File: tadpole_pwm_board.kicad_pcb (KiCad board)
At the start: 2 copper layers, 43.8 x 44.8 mm, 19 parts, among them J1 Conn_01x10_Socket, J10 Conn_01x04_Socket, J11 Conn_01x04_Socket, J9 Conn_01x06_Socket, SW1 SW_Push, SW2 SW_DIP_x06, U1 PCA9685PW, U3 ATtiny85-20S

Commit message: silkscreen work and remaining routing
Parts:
- added G***: LOGO, LOGO, B.Cu at (128.1, 111.3)
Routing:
- net GND: track 19.9 -> 29.1 mm, vias 10 -> 13
- net /RESET: track 39.3 -> 42.9 mm
- net +5V: track 0.00 -> 2.95 mm, vias 0 -> 2
- net /SCL/SCK: track 66.2 -> 64.4 mm
- net /A5: track 31.9 -> 32.8 mm
- net /PWM5: track 11.8 -> 12.6 mm
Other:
- board text added: "FLASH"
- board text added: "I2C ADDR"
- board text added: "PWM OUT"
- board text added: "RESET"
- board text added: "STEMMA"
- board text added: "SYSTEM FAILURE"
- board text added: "TODO: ADD LOGO CHOOSE SWITCH MOUNTING HOLES"
- board text added: "Tadpole ESC Driver Designed by Cooper Jones 9/26/2026"
- board text added: "{dblquote}I'ts me{dblquote}"
- board text removed: "Tadpole PWM thruster control board"

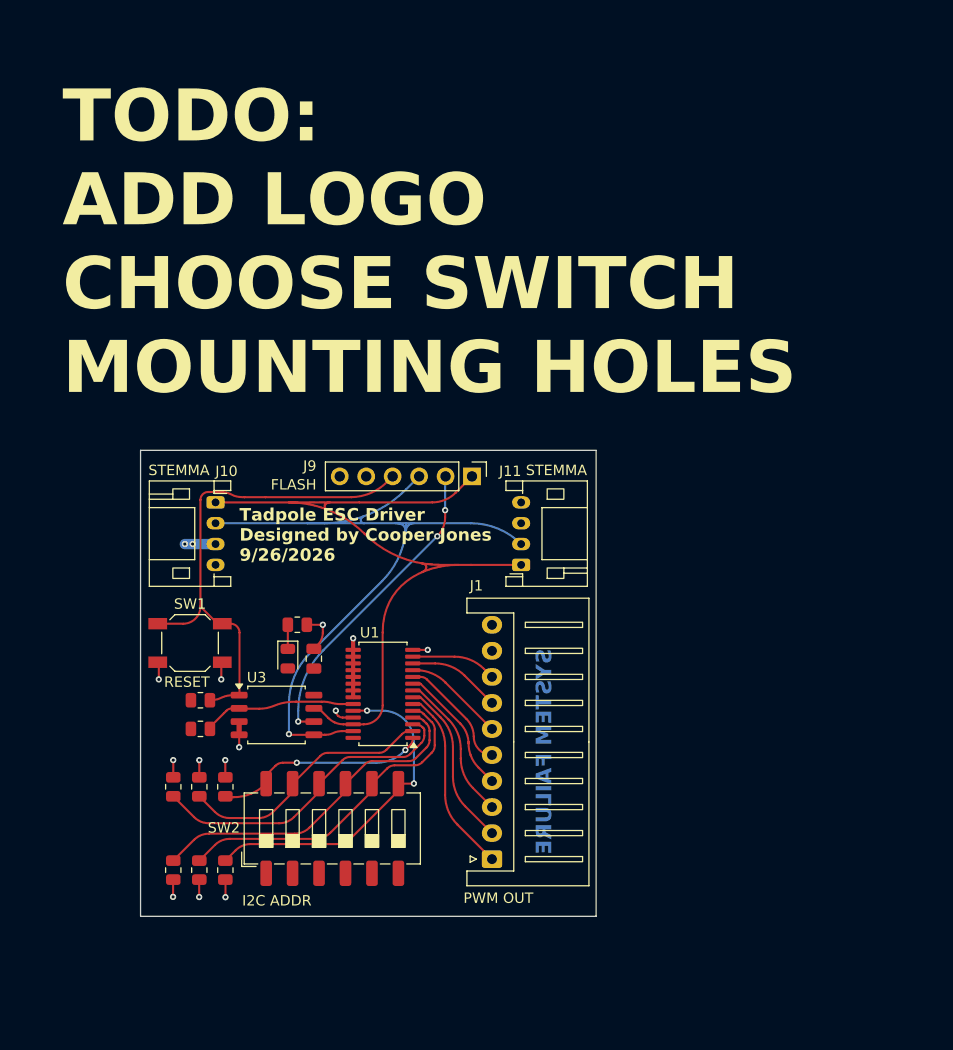
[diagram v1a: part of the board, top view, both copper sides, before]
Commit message: mounting holes, logos, labels, replaced switch
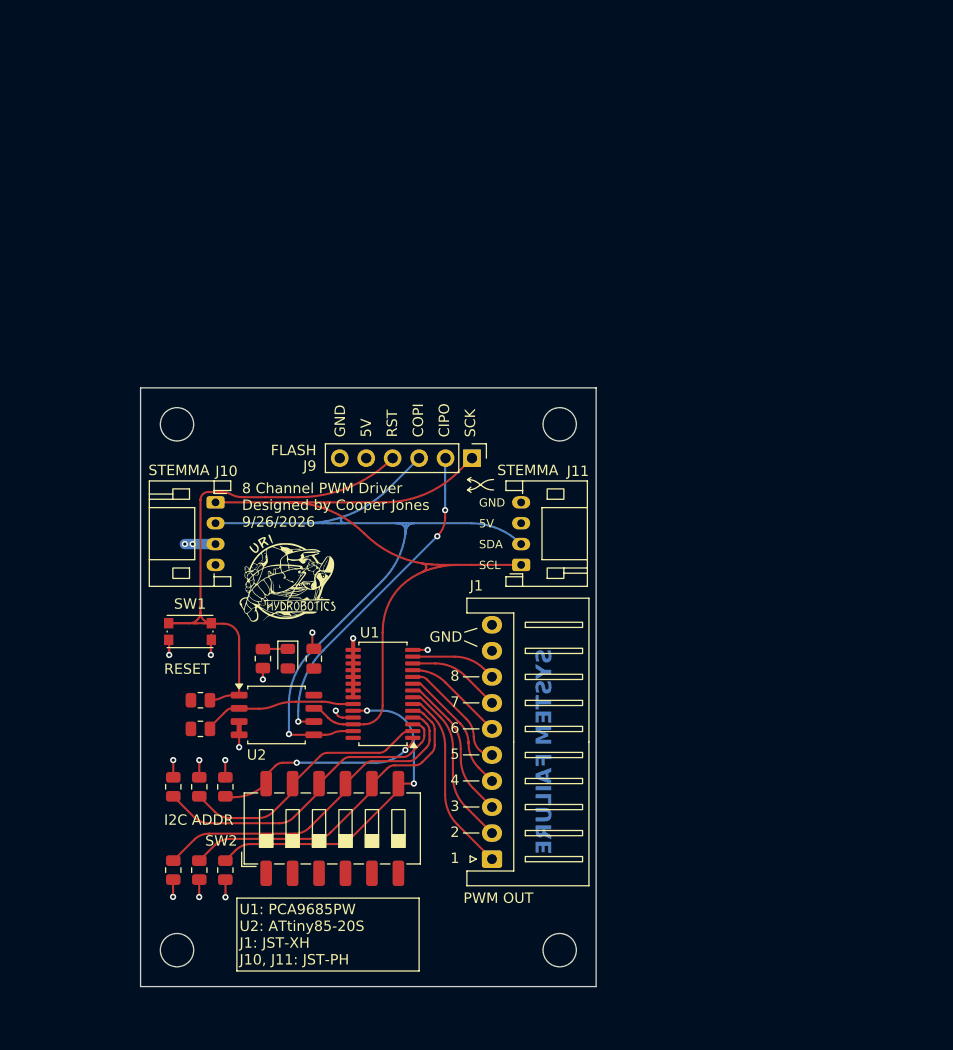
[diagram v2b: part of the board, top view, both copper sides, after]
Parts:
- added G***: LOGO, LOGO, F.Cu at (135.9, 90.2)
- added H1: MountingHole, MountingHole:MountingHole_3.2mm_M3, F.Cu at (125.8, 75.0)
- added H2: MountingHole, MountingHole:MountingHole_3.2mm_M3, F.Cu at (162.5, 75.0)
- added H3: MountingHole, MountingHole:MountingHole_3.2mm_M3, F.Cu at (125.8, 125.5)
- added H4: MountingHole, MountingHole:MountingHole_3.2mm_M3, F.Cu at (162.5, 125.5)
- SW1: footprint Button_Switch_SMD:SW_SPST_SKQG_WithoutStem -> Button_Switch_SMD:SW_Push_1P1T_NO_CK_KMR2
- moved R9 4.63 mm to (134.0, 97.5), turned to 90 degrees
- moved J9 1.75 mm to (154.1, 78.2)
- moved SW1 1.10 mm to (127.0, 94.9)
- renumbered U3 to U2
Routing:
- net /RESET: track 42.9 -> 46.5 mm
- net GND: track 29.1 -> 27.3 mm, vias 13 -> 14
- net /CIPO: track 30.4 -> 32.1 mm
- net /SDA/COPI: track 70.7 -> 71.9 mm
- added copper zone on F.Cu, net /RESET
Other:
- board size 43.8 x 44.8 mm -> 43.8 x 57.5 mm
- board text added: "1"
- board text added: "2"
- board text added: "3"
- board text added: "4"
- board text added: "5"
- board text added: "5V"
- board text added: "6"
- board text added: "7"
- board text added: "8"
- board text added: "8 Channel PWM Driver Designed by Cooper Jones 9/26/2026"
- board text added: "CIPO"
- board text added: "COPI"
- board text added: "GND"
- board text added: "RST"
- board text added: "SCK"
- board text added: "SCL"
- board text added: "SDA"
- board text added: "U1: PCA9685PW U2: ATtiny85-20S J1: JST-XH J10, J11: JST-PH"
- board text removed: "TODO: ADD LOGO CHOOSE SWITCH MOUNTING HOLES"
- board text removed: "Tadpole ESC Driver Designed by Cooper Jones 9/26/2026"

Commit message: added PB4 Led, and labeled 5V led
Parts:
- added D2: LED, LED_SMD:LED_0805_2012Metric, F.Cu at (128.8, 104.2)
- added R10: R_Small, Resistor_SMD:R_0805_2012Metric, F.Cu at (126.0, 103.5)
- moved R2 2.14 mm to (128.8, 102.2)
- moved R1 1.46 mm to (128.8, 100.2)
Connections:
- U2 pad 3: GND -> /LED2
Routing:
- net /RESET: track 46.5 -> 48.7 mm
- net Net-(D2-K): track 0.00 -> 1.85 mm
- net /OE: track 9.62 -> 8.03 mm
- net GND: track 27.3 -> 27.4 mm, vias 14 -> 15
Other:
- board text added: "JLCJLCJLCJLC"
- board text added: "PB4"

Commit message: swapped to 2x 4 pin headers
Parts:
- removed the J1 at (156.0, 116.8)
- added J4: Conn_01x04_Socket, Connector_JST:JST_XH_S4B-XH-A_1x04_P2.50mm_Horizontal, F.Cu at (155.9, 115.5)
- added J5: Conn_01x04_Socket, Connector_JST:JST_XH_S4B-XH-A_1x04_P2.50mm_Horizontal, F.Cu at (155.9, 101.7)
- renumbered J9 to J1, J10 to J2, J11 to J3
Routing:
- net /PWM5: track 12.6 -> 8.23 mm
- net /PWM6: track 9.76 -> 7.66 mm
- net /PWM1: track 18.1 -> 16.9 mm
- net /PWM7: track 8.99 -> 7.80 mm
- net /PWM2: track 16.2 -> 15.4 mm
- net /PWM3: track 14.3 -> 13.6 mm
